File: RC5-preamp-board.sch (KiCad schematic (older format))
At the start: 12 parts

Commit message: Schematic capture complete.
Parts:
- added C1, C2: 47u, ~, symbol CP1
- added C3: 100n, ~, symbol C
- added D1: 1N4007, ~, symbol DIODE
- added U1: NCP1117DT50RKG, DPAK, symbol LM7805CT
- gave numbers to parts that had none: 12
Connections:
- net labels added: RAW_DC
- wire segments 48 -> 65
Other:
- note added: "20 V max."
- note added: "Remove to use external VCC source."
- moved on the sheet: JP1, P1, P10, P2, P3, P4, P5, P6, P7, P8, P9

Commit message: Added IR receiver module to schematic. So it wasn't done after all. :-/
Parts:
- added R?: 330, ~, symbol R
- added U?: TSOP34136, ~, symbol IR_MOD
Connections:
- wire segments 65 -> 83
- no-connect marks 7 -> 6

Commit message: Schematic presentation refinements and corrected C4.
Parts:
- added C4: 100n, ~, symbol C
- R1: renamed from R?; value 330 -> 330R
- gave numbers to parts that had none: 1
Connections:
- wire segments 83 -> 74
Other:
- moved on the sheet: P10, P3, P9, R1, U3

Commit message: Changed from Pro Mini to discrete PCB implementation.
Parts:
- removed U2: ARDUINO_PRO_MINI, DIL24-600, symbol ARDUINO_PRO_MINI_24
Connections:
- net labels added: IR
- wire segments 74 -> 68
- no-connect marks 6 -> 3
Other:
- note added: "20 VDC max. raw input"
- note added: "Control signal outputs."
- note added: "External Vcc input."
- note added: "Requires current limiting resistors!!!"
- note added: "To (optional) indicator LEDs.\n"
- note added: "Vcc for external modules."
- note removed: "20 V max."
- note removed: "MUTE_SWITCH and PWR_SWITCH\nhave different pin assignments\nthan in the upstream project."
- moved on the sheet: C4, P10, P2, P3, P4, P5, P6, P7, P8, P9, R1, U3

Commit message: PCB placed, routability confirmed.
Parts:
- removed JP1: JUMPER, ~, symbol JUMPER
- removed U1: NCP1117DT50RKG, DPAK, symbol LM7805CT
- added U1: NCP1117DT50RKG, mfk-IPC7351-trans-TO228P1003X238-3N, symbol NCP1117
- C1, C2: footprint ~ -> mfk-CRP_5.0_2.0_0.5
- C3, C4: footprint ~ -> mfk-C_4.0_2.5_2.5_0.5
- D1: footprint ~ -> mfk-DO-41
- P1, P2, P4, P5, P6, P7, P9: footprint (none) -> mfk-SIL-2
- P10: footprint (none) -> mfk-SIL-6
- P3: renamed from P8; footprint (none) -> mfk-SIL-2
- P8: renamed from P3; footprint (none) -> mfk-SIL-7
- R1: footprint ~ -> mfk-R_0.25W_RN55
- U3: footprint ~ -> mfk-Vishay-TSOP341xx
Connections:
- net DGND: now also U1.1 (GND)
- net VCC: now also C2.1, C3.1, U1.2 (VOUT)
- net at C1.1, D1.2 (K): now also U1.3 (VIN)
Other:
- moved on the sheet: C2, C3, P3, P4, P5, P6, P7, U3

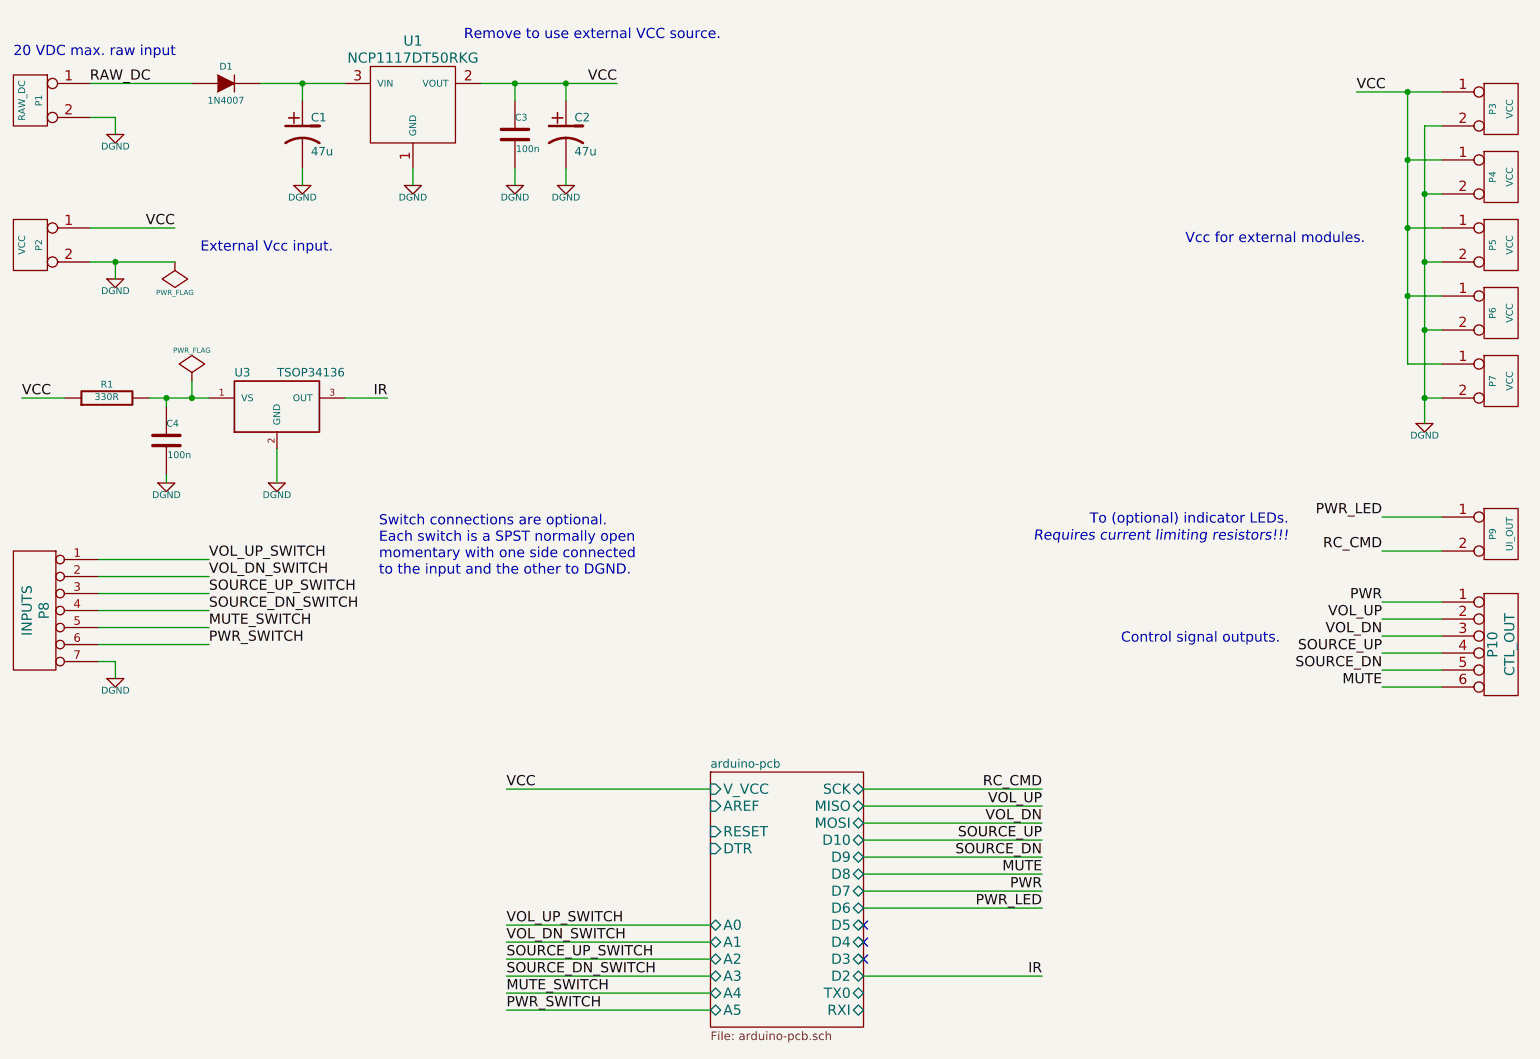
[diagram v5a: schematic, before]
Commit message: Removed one VCC tap. Keystone 621 mtg added. Routed.
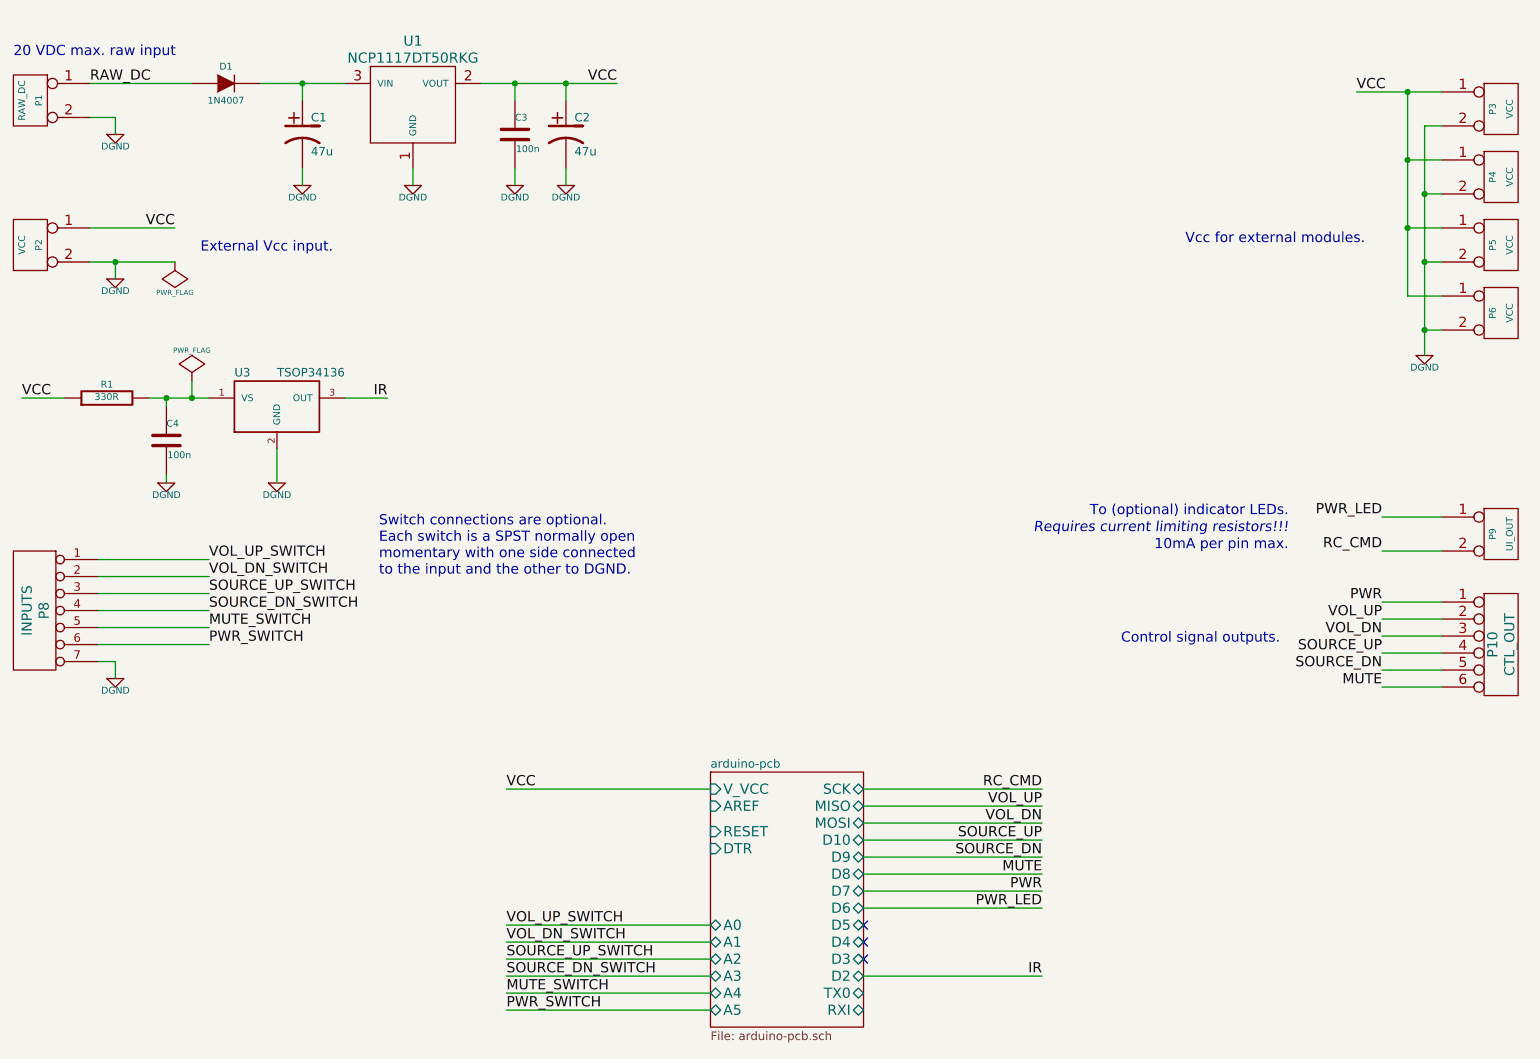
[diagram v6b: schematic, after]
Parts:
- removed P7: VCC, mfk-SIL-2, symbol CONN_2
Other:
- note added: "10mA per pin max."
- note removed: "Remove to use external VCC source."
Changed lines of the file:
@@
 Sheet 1 2
 Title "RC5 remote control board"
-Date "18 apr 2015"
+Date "19 apr 2015"
 Rev ""
 Comp "Mithat Konar"
@@
 $EndComp
 $Comp
-L CONN_2 P7
-U 1 1 55233AB2
-P 9700 2800
-F 0 "P7" V 9650 2800 40  0000 C CNN
-F 1 "VCC" V 9750 2800 40  0000 C CNN
-F 2 "mfk-SIL-2" H 9700 2800 60  0001 C CNN
-F 3 "" H 9700 2800 60  0000 C CNN
-	1    9700 2800
-	1    0    0    -1
-$EndComp
-$Comp
 L CONN_2 P3
 U 1 1 55233AB8
@@
 L DGND #PWR01
 U 1 1 55233AF1
-P 9250 3050
-F 0 "#PWR01" H 9250 3050 40  0001 C CNN
-F 1 "DGND" H 9250 2980 40  0000 C CNN
-F 2 "" H 9250 3050 60  0000 C CNN
-F 3 "" H 9250 3050 60  0000 C CNN
-	1    9250 3050
+P 9250 2650
+F 0 "#PWR01" H 9250 2650 40  0001 C CNN
+F 1 "DGND" H 9250 2580 40  0000 C CNN
+F 2 "" H 9250 2650 60  0000 C CNN
+F 3 "" H 9250 2650 60  0000 C CNN
+	1    9250 2650
 	1    0    0    -1
 $EndComp
@@
 Text Label 1900 1900 2    60   ~ 0
 VCC
-Text Notes 3600 800  0    60   ~ 0
-Remove to use external VCC source.
 $Comp
 L DGND #PWR04
@@
 63 98 05 E1 6B C4 72 91 8E EA 95 27 8C 4B 0B 6B 30 6B 95 2D 08 DF 47 79 14 D8 40 20 A9 90 96 2D
 E1 E7 3D C6 74 F3 E0 6E B9 00 E4 0E CC EC 2A 00 9E 03 F9 2E 43 53 93 3B E7 B1 3D FE 0F E4 2C B5
-B8 3A B8 3B 5D 00 00 00 00 49 45 4E 44 AE 42 60 82 82 $EndBitmap
+B8 3A B8 3B 5D 00 00 00 00 49 45 4E 44 AE 42 60 82 C8 $EndBitmap
 EndData
 $EndBitmap
@@
 	9350 1300 9250 1300
 Wire Wire Line
-	9250 1300 9250 3050
-Wire Wire Line
-	9350 2900 9250 2900
-Connection ~ 9250 2900
+	9250 1300 9250 2650
 Wire Wire Line
 	9350 2500 9250 2500
@@
 Connection ~ 9250 1700
 Wire Wire Line
-	9150 2700 9350 2700
-Wire Wire Line
 	8850 1100 9350 1100
 Wire Wire Line
-	9150 1100 9150 2700
-Wire Wire Line
-	9350 2300 9150 2300
-Connection ~ 9150 2300
+	9150 2300 9350 2300
 Wire Wire Line
 	9350 1900 9150 1900
@@
 NoConn ~ 5950 6100
 NoConn ~ 5950 6200
-Text Notes 8450 3650 2    60   ~ 0
+Text Notes 8450 3600 2    60   ~ 0
 To (optional) indicator LEDs.\n
-Text Notes 8450 3750 2    60   Italic 0
+Text Notes 8450 3700 2    60   Italic 0
 Requires current limiting resistors!!!
 Text Notes 8900 2000 2    60   ~ 0
@@
 Wire Wire Line
 	3700 1050 4500 1050
+Text Notes 8450 3800 2    60   ~ 0
+10mA per pin max.
+Wire Wire Line
+	9150 1100 9150 2300
 $EndSCHEMATC

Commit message: Nudged TSOP receiver back so the main body is just a hair recessed from PCB edge.
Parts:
- U3: footprint mfk-Vishay-TSOP341xx -> mfk-Vishay-TSOP341xx-alt
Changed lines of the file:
@@
 Sheet 1 2
 Title "RC5 remote control board"
-Date "19 apr 2015"
+Date "20 apr 2015"
 Rev ""
 Comp "Mithat Konar"
@@
 63 98 05 E1 6B C4 72 91 8E EA 95 27 8C 4B 0B 6B 30 6B 95 2D 08 DF 47 79 14 D8 40 20 A9 90 96 2D
 E1 E7 3D C6 74 F3 E0 6E B9 00 E4 0E CC EC 2A 00 9E 03 F9 2E 43 53 93 3B E7 B1 3D FE 0F E4 2C B5
-B8 3A B8 3B 5D 00 00 00 00 49 45 4E 44 AE 42 60 82 C8 $EndBitmap
+B8 3A B8 3B 5D 00 00 00 00 49 45 4E 44 AE 42 60 82 A0 $EndBitmap
 EndData
 $EndBitmap
@@
 F 0 "U3" H 2250 3250 50  0000 L CNN
 F 1 "TSOP34136 " H 2700 3250 50  0000 C CNN
-F 2 "mfk-Vishay-TSOP341xx" H 2500 2900 60  0001 C CNN
+F 2 "mfk-Vishay-TSOP341xx-alt" H 2500 2900 60  0001 C CNN
 F 3 "~" H 2500 2900 60  0000 C CNN
 	1    2500 3000
